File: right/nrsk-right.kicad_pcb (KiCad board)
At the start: 2 copper layers, 180.5 x 133.5 mm, 135 parts, among them J1 USB-C, J2 USB-C, J3 OLED 128x32, SW1 F7, SW10 0, SW11 -, SW12 =, SW13 Backspace, SW14 Y, SW15 U, SW16 I, SW17 O, SW18 P, SW19 [, SW2 F8, SW20 ], SW21 \, SW22 H, SW23 J, SW24 K, SW25 L, SW26 ;, SW27 ', SW28 Enter, SW29 N, SW3 F9, SW30 M, SW31 ,, SW32 ., SW33 /, SW34 ↑, SW35 fn, SW36 Space, SW37 Space, SW38 Cmd, SW39 Opt, SW4 F10, SW40 ←, SW41 ↓, SW42 →, SW5 F11, SW6 F12, SW7 7, SW8 8, SW9 9, U1 RP2040, U2 USBLC6-2SC6, U4 AP2112K-3.3, U5 W25Q128JVS, Y1 12MHz

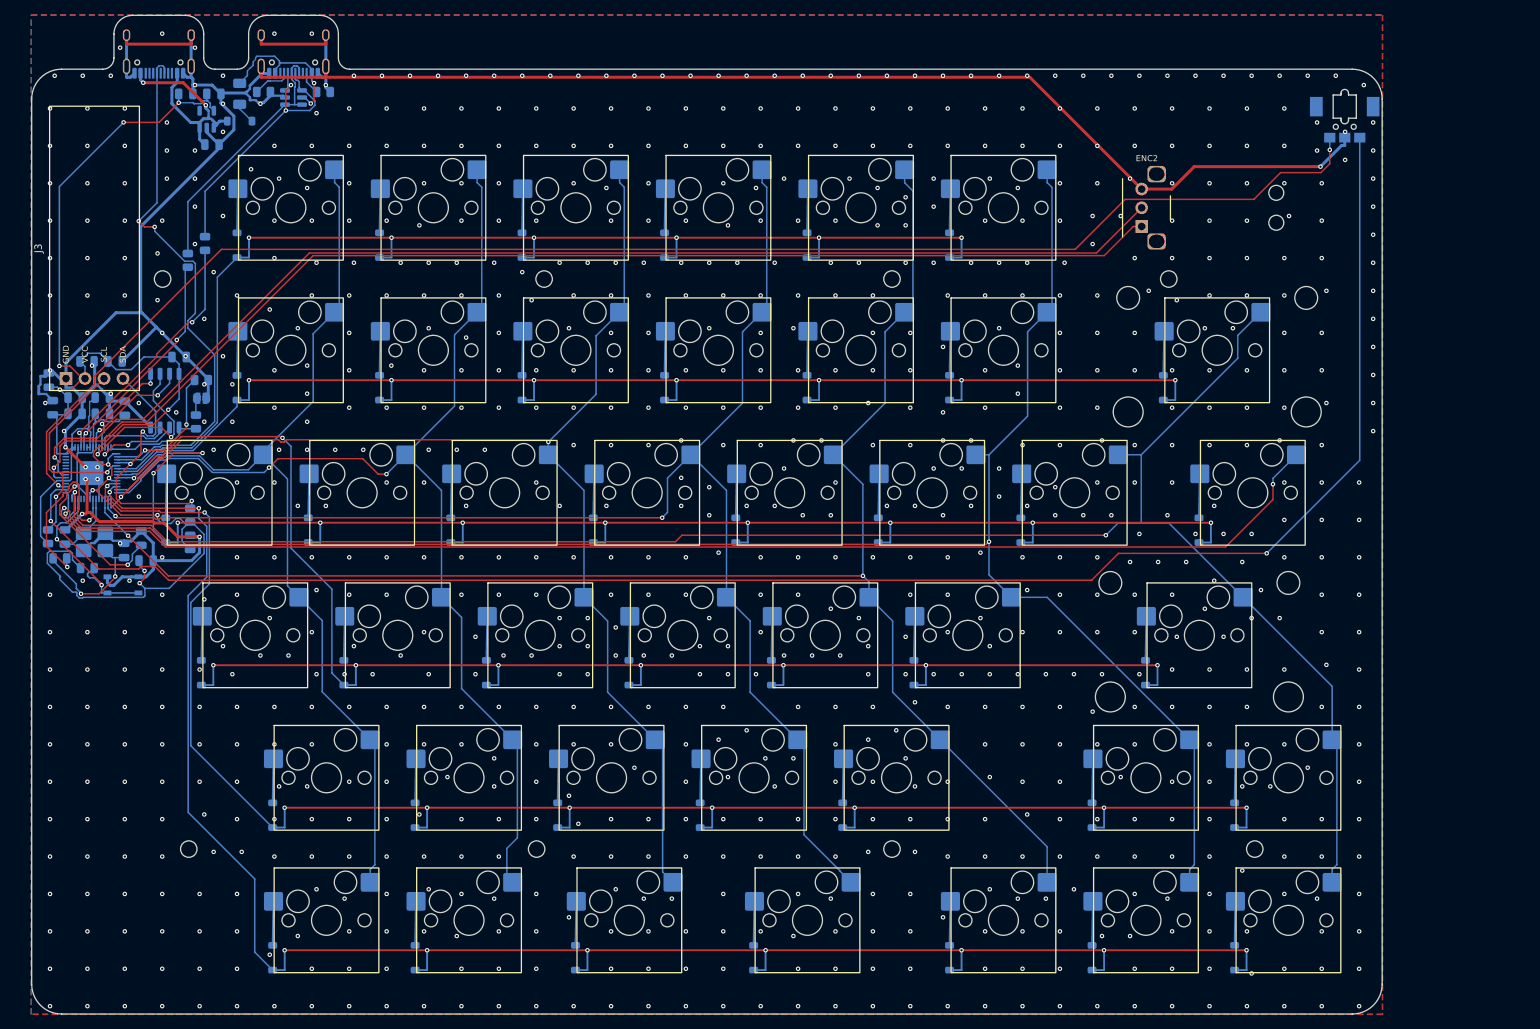
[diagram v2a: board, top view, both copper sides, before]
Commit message: Drum dial: widen the drum to 1.25 u (23.8 mm), bezel centred on Backspace
The free 2 u above Backspace now holds the widest drum it can: with the encoder (6.1 mm) and the
bearing block (3 mm) beside it, 1.5 u would need 38.5 mm and the encoder hood would sit on the F12
switch. The drum width lives in gen/footprints.py (DRUM_W) and the PCB, the case and the renders read it.
The drum sits 1.75 mm right of Backspace's centre so the bezel (longer hood on the encoder side) is
centred on the key; the bezel's snap hooks move to the middle of the drum.
Right board re-routed (0 unconnected, 0 parity issues); case checks pass. README, spec and BOM updated.

Co-Authored-By: Claude Opus 5.5 <noreply@anthropic.com>
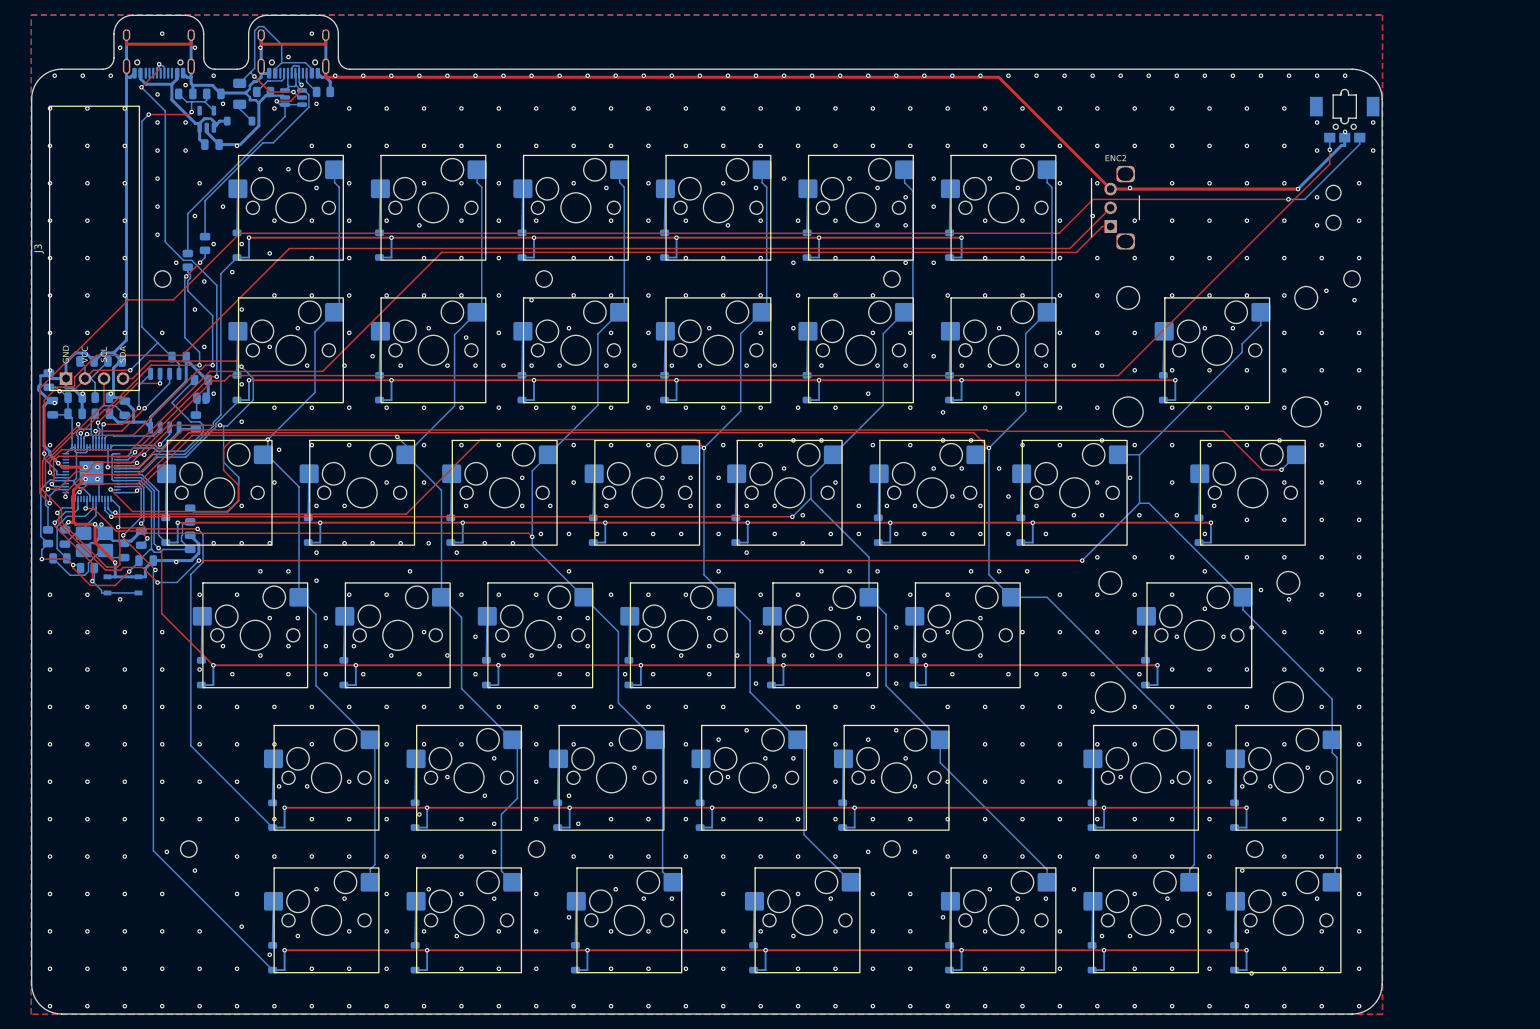
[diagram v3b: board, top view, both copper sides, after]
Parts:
- moved H4 24.5 mm to (203.5, 49.0)
- moved DRUM1 4.15 mm to (174.9, 39.5)
- moved ENC2 4.15 mm to (174.9, 39.5)
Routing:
- net /3V3: track 216.9 -> 163.7 mm, vias 11 -> 7
- net /ROW3: track 216.9 -> 188.2 mm, vias 9 -> 8
- net /SDA: track 35.1 -> 62.1 mm
- net /ENC_A: track 234.1 -> 210.2 mm
- net /1V1: track 39.4 -> 58.4 mm, vias 2 -> 3
- net /ROW2: track 202.4 -> 185.8 mm, vias 10 -> 8
- net /XOUT: track 25.2 -> 11.9 mm, vias 2 -> 0
- net /COL0: track 129.3 -> 140.3 mm, vias 0 -> 2
- net /VBUS: track 20.8 -> 30.1 mm
- net VCC: track 30.4 -> 22.3 mm, vias 2 -> 0
- net /QSPI_SCLK: track 22.9 -> 15.2 mm
- net GND: track 407.2 -> 399.6 mm, vias 893 -> 898
- net /D+: track 29.8 -> 37.5 mm
- net /SCL: track 33.4 -> 40.3 mm
- net /COL4: track 218.6 -> 211.7 mm
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
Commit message: Move the RP2040 and its support parts to the front, visible through the clear plate
- RP2040, flash, crystal, LDO, decoupling caps and resistors on the front, in the
  key-free strip along the inner edge (clear of every keycap and the OLED cover);
  USB-C and its protection parts, reset switch and BOOTSEL pad stay on the back
- RP2040 fixed with pin 1 top-left so its Raspberry Pi logo reads upright
  (datasheet Figure 168); make_pcb asserts the orientation
- Left half: pin row 1-14 faces the keys, so it is fanned out to 1 mm pitch and
  the matrix rows are routed by make_pcb; Freerouting does the rest
- build.sh retries routing until 0 unconnected and 0 DRC violations
- USB-C footprint copy in lib/nrsk.pretty with its outline on Fab (no clipped silk)
- JLC CPL handles top-side parts; front assembly drawing added
- Printed plate B: web cut away over the front-side parts
- DRC (all severities) 0, unconnected 0, parity 0, ERC 0 on both halves
- Docs, renders, fab outputs and case files regenerated

Co-Authored-By: Claude Opus 5.5 <noreply@anthropic.com>
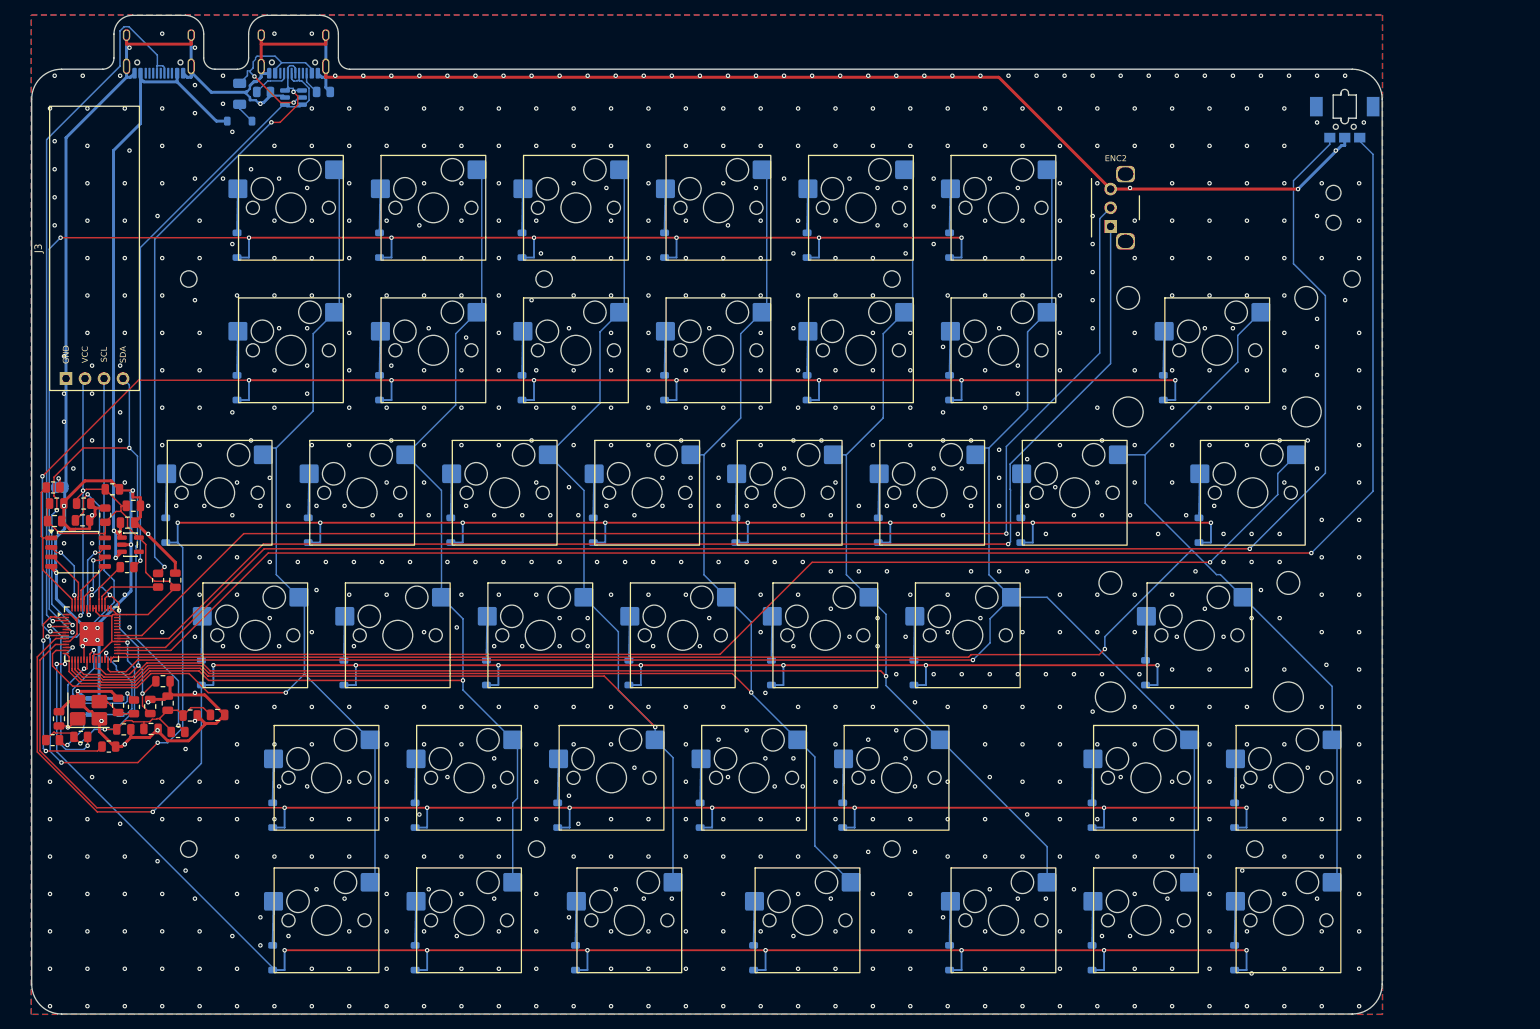
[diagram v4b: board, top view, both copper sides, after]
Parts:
- C1, C11, C12, C13, C14, C15, C16, C17, C18, C19, C2, C20, C3, C4, C5, C6, C7, C8, R1, R10, R2, R3, R6, R7, R8, R9, U1, U4, U5, Y1: moved to F.Cu
- J1, J2: footprint Connector_USB:USB_C_Receptacle_HRO_TYPE-C-31-M-12 -> nrsk:USB_C_Receptacle_HRO_TYPE-C-31-M-12
- moved U4 57.8 mm to (40.2, 84.6), turned to 0 degrees
- moved C19 57.3 mm to (36.8, 80.6), turned to 90 degrees
- moved C17 56.1 mm to (40.6, 79.4)
- moved C16 51.8 mm to (39.8, 81.6)
- moved R1 50.5 mm to (37.3, 111.5)
- moved C18 49.2 mm to (51.9, 107.3)
- moved R3 45.4 mm to (43.9, 89.3)
- moved C13 45.2 mm to (48.2, 107.4)
- moved C12 42.4 mm to (45.2, 105.8)
- moved R2 41.8 mm to (39.8, 87.6), turned to 0 degrees
- moved C4 36.7 mm to (44.5, 102.8)
- moved R9 29.0 mm to (46.6, 109.6), turned to 0 degrees
- moved R8 27.1 mm to (33.6, 110.2), turned to 0 degrees
- moved C8 26.5 mm to (39.3, 109.2), turned to 0 degrees
- moved C3 26.0 mm to (46.2, 89.3), turned to 90 degrees
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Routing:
- net VCC: track 22.3 -> 86.4 mm, vias 0 -> 2
- net /ROW2: track 185.8 -> 235.4 mm, vias 8 -> 11
- net /USB_D-: track 33.0 -> 81.7 mm, vias 0 -> 3
- net /USB_D+: track 38.0 -> 80.3 mm, vias 2 -> 1
- net /ROW0: track 159.8 -> 201.7 mm, vias 6 -> 8
- net /ROW1: track 174.0 -> 209.9 mm, vias 7 -> 9
- net GND: track 399.6 -> 431.0 mm, vias 898 -> 880
- net /D+: track 37.5 -> 6.68 mm, vias 2 -> 0
- net /D-: track 38.9 -> 9.61 mm, vias 4 -> 0
- net /DATA: track 68.4 -> 96.1 mm, vias 4 -> 1
- net /ENC_B: track 195.8 -> 219.8 mm, vias 2 -> 1
- net /ROW3: track 188.2 -> 211.9 mm
- net /SCL: track 40.3 -> 63.9 mm
- net /SDA: track 62.1 -> 84.9 mm, vias 3 -> 4
- net /COL2: track 168.6 -> 190.7 mm, vias 2 -> 1
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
